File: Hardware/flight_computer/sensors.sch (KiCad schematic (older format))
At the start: 4 parts

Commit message: added parts for DAN <3
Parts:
- J?: symbol openDrone_parts:DF40C2.0-20DS-0.4V51 -> flight_computer-rescue:DF40C2.0-20DS-0.4V51-openDrone_parts
- U?: symbol openDrone_parts:LIS3MDLTR -> flight_computer-rescue:LIS3MDLTR-openDrone_parts
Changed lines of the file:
@@
 Connection ~ 7800 5000
 $Comp
-L openDrone_parts:DF40C2.0-20DS-0.4V51 J?
+L flight_computer-rescue:DF40C2.0-20DS-0.4V51-openDrone_parts J?
 U 1 1 5F6366CC
 P 2800 5150
@@
 	4500 6050 3500 6050
 $Comp
-L openDrone_parts:LIS3MDLTR U?
+L flight_computer-rescue:LIS3MDLTR-openDrone_parts U?
 U 1 1 5F647DF8
 P 7300 2500

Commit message: added more parts and datasheets
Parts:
- J?: symbol flight_computer-rescue:DF40C2.0-20DS-0.4V51-openDrone_parts -> flight_computer-rescue:DF40C2.0-20DS-0.4V51-openDrone_parts-flight_computer-rescue
- U?: symbol flight_computer-rescue:LIS3MDLTR-openDrone_parts -> flight_computer-rescue:LIS3MDLTR-openDrone_parts-flight_computer-rescue
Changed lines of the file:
@@
 Connection ~ 7800 5000
 $Comp
-L flight_computer-rescue:DF40C2.0-20DS-0.4V51-openDrone_parts J?
+L flight_computer-rescue:DF40C2.0-20DS-0.4V51-openDrone_parts-flight_computer-rescue J?
 U 1 1 5F6366CC
 P 2800 5150
@@
 	4500 6050 3500 6050
 $Comp
-L flight_computer-rescue:LIS3MDLTR-openDrone_parts U?
+L flight_computer-rescue:LIS3MDLTR-openDrone_parts-flight_computer-rescue U?
 U 1 1 5F647DF8
 P 7300 2500

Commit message: Adds sensors
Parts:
- removed J?: DF40C2.0-20DS-0.4V51, drone_footprints:DF40C2.0-20DS-0.4V51, symbol flight_computer-rescue:DF40C2.0-20DS-0.4V51-openDrone_parts-flight_computer-res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
- removed U?: MPU-6000, Sensor_Motion:InvenSense_QFN-24_4x4mm_P0.5mm, symbol Sensor_Motion:MPU-6000
- removed U?: MS5611-01BA, Package_LGA:LGA-8_3x5mm_P1.25mm, symbol Sensor_Pressure:MS5611-01BA
- removed U?: LIS3MDLTR, drone_footprints:LIS3MDLTR, symbol flight_computer-rescue:LIS3MDLTR-openDrone_parts-flight_computer-rescue
- added C? (x6): C_0u1, Capacitors_SMD:C_0805, symbol openDrone_parts:C_0u1
- added C?: C_1u, Capacitors_SMD:C_0805, symbol openDrone_parts:C_1u
- added C?: C_10u, Capacitors_SMD:C_0805, symbol openDrone_parts:C_10u
- added C?: C_2u2, Capacitors_SMD:C_0805, symbol openDrone_parts:C_2u2
- added R?: R_220, Resistors_SMD:R_0805, symbol openDrone_parts:R_220
- added U?: BMI088, drone_footprints:BMI088, symbol openDrone_parts:BMI088
- added U?: LIS3MDLTR, drone_footprints:LIS3MDLTR, symbol openDrone_parts:LIS3MDLTR
- added U?: Barometer, drone_footprints:MS561101BA03-50, symbol openDrone_parts:Barometer
- added U?: LP5907QMFX-3.3, TO_SOT_Packages_SMD:SOT-23-5, symbol openDrone_parts:LP5907QMFX-3.3
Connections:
- net labels added: BARO_MISO, BARO_MOSI, BARO_SCK, CSB_ACCEL, CSB_GYRO, IMU_INT1_ACCEL, IMU_INT2_ACCEL, IMU_MISO, IMU_MOSI, IMU_SCK, INT3_GYRO, INT4_GYRO, MAG_CS, MAG_DRDY, MAG_INT, MAG_SCL, MAG_SDA_SDI_SDO, MAG_SDO_SA1, VDDIO, VDD_3V3_SENSORS_EN, VDD_5V
- net labels removed: ACCEL_MAG_EXT_CS, BARO_EXT_CS, GYRO_EXT_CS, IMU_TEMPERATURE_CONTROL, MPU_CS, MPU_EXT_CS, SPI_EXT_MISO, SPI_EXT_MOSI, SPI_EXT_SCK, SPI_INT_MISO, SPI_INT_MOSI, SPI_INT_SCK
- wire segments 43 -> 53

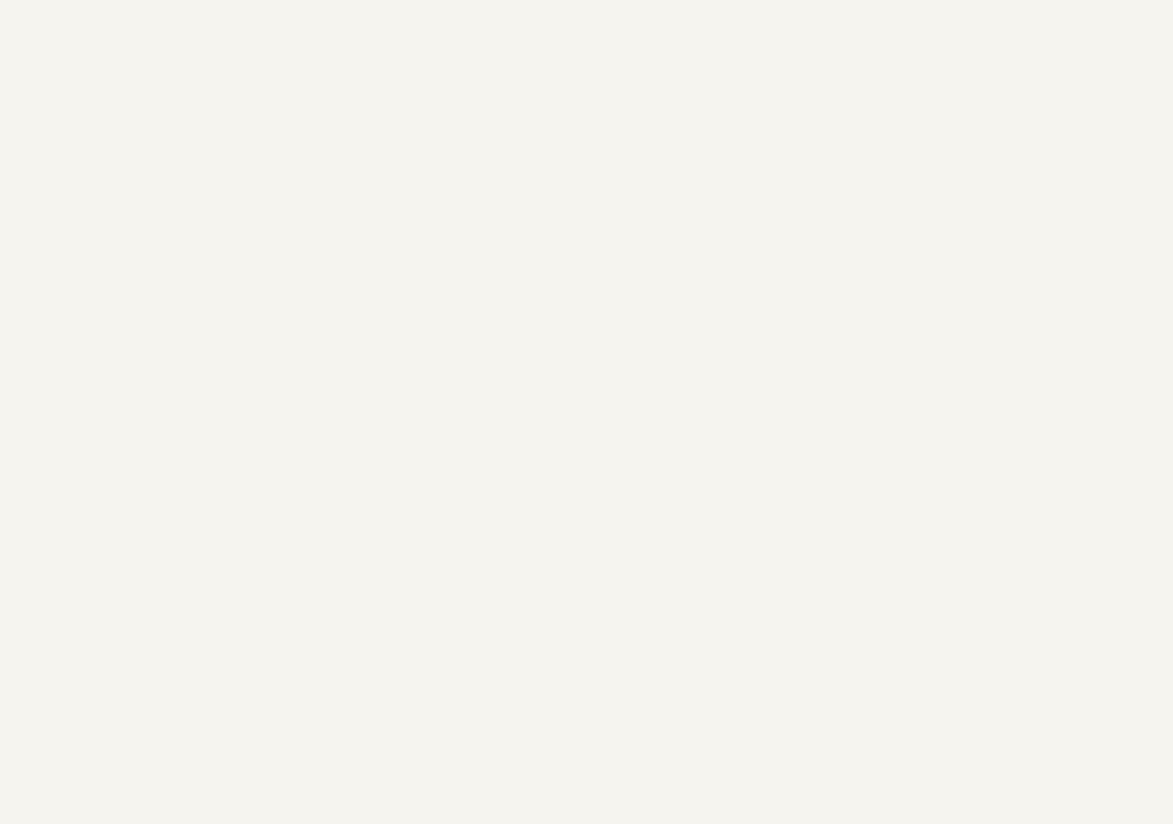
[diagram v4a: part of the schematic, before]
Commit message: Adds more sensor connections and communication with stm
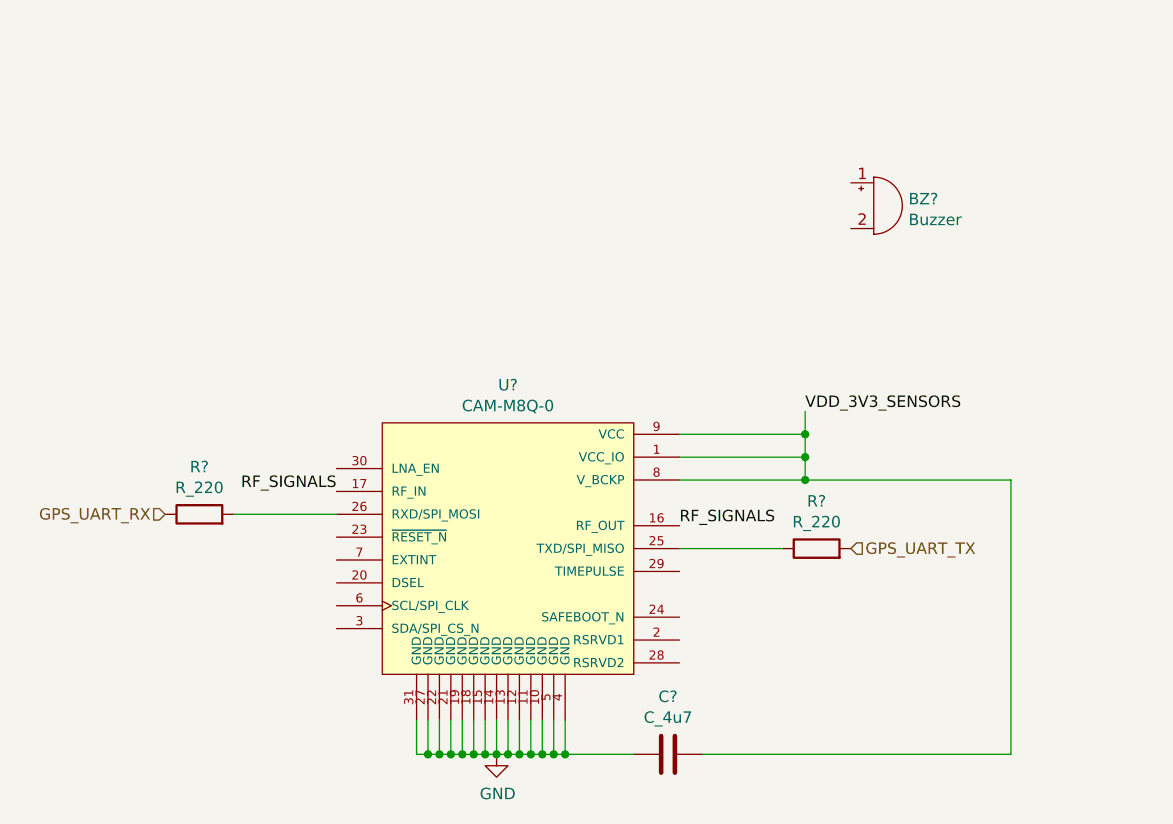
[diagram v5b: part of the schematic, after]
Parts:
- added BZ?: Buzzer, drone_footprints:PT-2040PQ, symbol openDrone_parts:Buzzer
- added C?: C_4u7, Capacitors_SMD:C_0805, symbol openDrone_parts:C_4u7
- added R? (x2): R_220, Resistors_SMD:R_0805, symbol openDrone_parts:R_220
- added U?: CAM-M8Q-0, drone_footprints:CAM_M8Q_0, symbol openDrone_parts:CAM-M8Q-0
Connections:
- net GND: now also C?.2, U?.10 (GND), U?.11 (GND), U?.12 (GND), U?.13 (GND), U?.14 (GND), U?.15 (GND), U?.18 (GND), U?.19 (GND), U?.21 (GND), U?.22 (GND), U?.27 (GND), U?.31 (GND), U?.4 (GND), U?.5 (GND)
- net VDD_3V3_SENSORS: now also C?.1, U?.1 (VCC_IO), U?.8 (V_BCKP), U?.9 (VCC)
- new net: R?.1, U?.25 (TXD/SPI_MISO)
- new net: R?.2, U?.26 (RXD/SPI_MOSI)
- new net GPS_UART_RX: R?.1
- new net GPS_UART_TX: R?.2
- new net RF_SIGNALS: U?.16 (RF_OUT), U?.17 (RF_IN)
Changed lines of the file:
@@
 $Descr A4 11693 8268
 encoding utf-8
-Sheet 2 5
+Sheet 2 4
 Title ""
 Date ""
@@
 Text Label 10400 4150 0    50   ~ 0
 VDD_3V3_SENSORS
+$Comp
+L openDrone_parts:Buzzer BZ?
+U 1 1 5F827564
+P 4700 3500
+F 0 "BZ?" H 4852 3529 50  0000 L CNN
+F 1 "Buzzer" H 4852 3438 50  0000 L CNN
+F 2 "drone_footprints:PT-2040PQ" H 5050 3950 50  0001 C CNN
+F 3 "~" V 4675 3600 50  0001 C CNN
+F 4 "458-1078-ND" H 5000 3750 50  0001 C CNN "DPN"
+F 5 "PT-2040PQ" H 4950 3850 50  0001 C CNN "MPN"
+	1    4700 3500
+	1    0    0    -1
+$EndComp
+$Comp
+L openDrone_parts:CAM-M8Q-0 U?
+U 1 1 5F827FBC
+P 3100 4600
+F 0 "U?" H 3100 4915 50  0000 C CNN
+F 1 "CAM-M8Q-0" H 3100 4824 50  0000 C CNN
+F 2 "drone_footprints:CAM_M8Q_0" H 2650 4950 50  0001 L BNN
+F 3 "UBlox" H 3000 4850 50  0001 L BNN
+F 4 "672-CAM-M8Q-0CT-ND" H 3150 4850 50  0001 C CNN "DPN"
+	1    3100 4600
+	1    0    0    -1
+$EndComp
+$Comp
+L openDrone_parts:R_220 R?
+U 1 1 5F82A212
+P 4450 5000
+F 0 "R?" H 4450 5207 50  0000 C CNN
+F 1 "R_220" H 4450 5116 50  0000 C CNN
+F 2 "Resistors_SMD:R_0805" H 3650 5150 50  0001 C CNN
+F 3 "" H 4150 5500 50  0001 C CNN
+F 4 "311-220CRCT-ND" H 3800 5250 60  0001 C CNN "DPN"
+	1    4450 5000
+	1    0    0    -1
+$EndComp
+$Comp
+L openDrone_parts:R_220 R?
+U 1 1 5F82B7EB
+P 1750 4850
+F 0 "R?" H 1750 5057 50  0000 C CNN
+F 1 "R_220" H 1750 4966 50  0000 C CNN
+F 2 "Resistors_SMD:R_0805" H 950 5000 50  0001 C CNN
+F 3 "" H 1450 5350 50  0001 C CNN
+F 4 "311-220CRCT-ND" H 1100 5100 60  0001 C CNN "DPN"
+	1    1750 4850
+	1    0    0    -1
+$EndComp
+Text HLabel 4600 5000 2    50   Input ~ 0
+GPS_UART_TX
+Text HLabel 1600 4850 0    50   Input ~ 0
+GPS_UART_RX
+$Comp
+L power:GND #PWR?
+U 1 1 5F857A76
+P 3050 5900
+F 0 "#PWR?" H 3050 5650 50  0001 C CNN
+F 1 "GND" H 3055 5727 50  0000 C CNN
+F 2 "" H 3050 5900 50  0001 C CNN
+F 3 "" H 3050 5900 50  0001 C CNN
+	1    3050 5900
+	1    0    0    -1
+$EndComp
+Wire Wire Line
+	2700 5750 2700 5900
+Wire Wire Line
+	2700 5900 2750 5900
+Wire Wire Line
+	3350 5750 3350 5900
+Wire Wire Line
+	3350 5900 3300 5900
+Connection ~ 3050 5900
+Wire Wire Line
+	3300 5750 3300 5900
+Connection ~ 3300 5900
+Wire Wire Line
+	3300 5900 3250 5900
+Wire Wire Line
+	3250 5750 3250 5900
+Connection ~ 3250 5900
+Wire Wire Line
+	3250 5900 3200 5900
+Wire Wire Line
+	3200 5750 3200 5900
+Connection ~ 3200 5900
+Wire Wire Line
+	3200 5900 3150 5900
+Wire Wire Line
+	3150 5750 3150 5900
+Connection ~ 3150 5900
+Wire Wire Line
+	3150 5900 3100 5900
+Wire Wire Line
+	3100 5750 3100 5900
+Connection ~ 3100 5900
+Wire Wire Line
+	3100 5900 3050 5900
+Wire Wire Line
+	3050 5750 3050 5900
+Wire Wire Line
+	3000 5750 3000 5900
+Connection ~ 3000 5900
+Wire Wire Line
+	3000 5900 3050 5900
+Wire Wire Line
+	2950 5750 2950 5900
+Connection ~ 2950 5900
+Wire Wire Line
+	2950 5900 3000 5900
+Wire Wire Line
+	2900 5750 2900 5900
+Connection ~ 2900 5900
+Wire Wire Line
+	2900 5900 2950 5900
+Wire Wire Line
+	2850 5750 2850 5900
+Connection ~ 2850 5900
+Wire Wire Line
+	2850 5900 2900 5900
+Wire Wire Line
+	2800 5750 2800 5900
+Connection ~ 2800 5900
+Wire Wire Line
+	2800 5900 2850 5900
+Wire Wire Line
+	2750 5750 2750 5900
+Connection ~ 2750 5900
+Wire Wire Line
+	2750 5900 2800 5900
+Text Label 2350 4750 2    50   ~ 0
+RF_SIGNALS
+Wire Wire Line
+	1900 4850 2350 4850
+Text Label 3850 4900 0    50   ~ 0
+RF_SIGNALS
+Wire Wire Line
+	3850 5000 4300 5000
+Text Label 4400 4400 0    50   ~ 0
+VDD_3V3_SENSORS
+Wire Wire Line
+	3850 4500 4400 4500
+Wire Wire Line
+	4400 4500 4400 4400
+Wire Wire Line
+	3850 4600 4400 4600
+Wire Wire Line
+	4400 4600 4400 4500
+Connection ~ 4400 4500
+Wire Wire Line
+	3850 4700 4400 4700
+Wire Wire Line
+	4400 4700 4400 4600
+Connection ~ 4400 4600
+$Comp
+L openDrone_parts:C_4u7 C?
+U 1 1 5F87B412
+P 3800 5900
+F 0 "C?" V 3548 5900 50  0000 C CNN
+F 1 "C_4u7" V 3639 5900 50  0000 C CNN
+F 2 "Capacitors_SMD:C_0805" H 3838 5750 50  0001 C CNN
+F 3 "" H 3825 6000 50  0001 C CNN
+F 4 "490-14466-1-ND" H 3800 5900 60  0001 C CNN "DPN"
+	1    3800 5900
+	0    1    1    0
+$EndComp
+Wire Wire Line
+	3350 5900 3650 5900
+Connection ~ 3350 5900
+Wire Wire Line
+	3950 5900 5300 5900
+Wire Wire Line
+	5300 5900 5300 4700
+Wire Wire Line
+	5300 4700 4400 4700
+Connection ~ 4400 4700
 $EndSCHEMATC

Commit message: Updates drdy pins and rc connections
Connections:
- net IMU_INT2_ACCEL: no longer names the net of U?.1 (INT2)
- net INT4_GYRO: no longer names the net of U?.13 (INT4)
- net MAG_INT: no longer names the net of U?.7 (INT)
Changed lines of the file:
@@
 Text HLabel 3850 1000 2    50   Input ~ 0
 IMU_INT1_ACCEL
-Text HLabel 3850 1100 2    50   Input ~ 0
-IMU_INT2_ACCEL
 Text HLabel 3850 1200 2    50   Input ~ 0
 INT3_GYRO
-Text HLabel 3850 1300 2    50   Input ~ 0
-INT4_GYRO
 Wire Wire Line
 	3850 1500 3950 1500
@@
 	2700 2450 2900 2450
 Connection ~ 2900 2450
-$Comp
-L openDrone_parts:LIS3MDLTR U?
-U 1 1 5F9477A8
-P 6450 1150
-F 0 "U?" H 7400 1437 60  0000 C CNN
-F 1 "LIS3MDLTR" H 7400 1331 60  0000 C CNN
-F 2 "drone_footprints:LIS3MDLTR" H 7650 1390 60  0001 C CNN
-F 3 "https://www.st.com/content/ccc/resource/technical/document/datasheet/54/2a/85/76/e3/97/42/18/DM00075867.pdf/files/DM00075867.pdf/jcr:content/translations/en.DM00075867.pdf" H 6450 1150 60  0001 C CNN
-F 4 "497-13892-1-ND" H 8400 1500 50  0001 C CNN "DPN"
-	1    6450 1150
-	1    0    0    -1
-$EndComp
 Text HLabel 6450 1650 0    50   Input ~ 0
 VDDIO
@@
 Text HLabel 8350 1550 2    50   Input ~ 0
 MAG_DRDY
-Text HLabel 8350 1650 2    50   Input ~ 0
-MAG_INT
 Text HLabel 8350 1350 2    50   Input ~ 0
 MAG_CS
@@
 	5300 4700 4400 4700
 Connection ~ 4400 4700
+$Comp
+L openDrone_parts:LIS3MDLTR U?
+U 1 1 5F9477A8
+P 6450 1150
+F 0 "U?" H 7400 1437 60  0000 C CNN
+F 1 "LIS3MDLTR" H 7400 1331 60  0000 C CNN
+F 2 "drone_footprints:LIS3MDLTR" H 7650 1390 60  0001 C CNN
+F 3 "https://www.st.com/content/ccc/resource/technical/document/datasheet/54/2a/85/76/e3/97/42/18/DM00075867.pdf/files/DM00075867.pdf/jcr:content/translations/en.DM00075867.pdf" H 6450 1150 60  0001 C CNN
+F 4 "497-13892-1-ND" H 8400 1500 50  0001 C CNN "DPN"
+	1    6450 1150
+	1    0    0    -1
+$EndComp
 $EndSCHEMATC

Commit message: Adds buck converters
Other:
- note added: "GPS\n<71mA, avg <26mA"
- note added: "IMU\n150uA"
- note added: "Magnetometer\n40-270uA"
- note added: "barometer\n<1.4mA"
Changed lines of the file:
@@
 	1    0    0    -1
 $EndComp
+Text Notes 7100 2000 0    50   ~ 0
+Magnetometer\n40-270uA
+Text Notes 3900 1800 0    50   ~ 0
+IMU\n150uA
+Text Notes 1750 5750 0    50   ~ 0
+GPS\n<71mA, avg <26mA
+Text Notes 9150 3500 0    50   ~ 0
+barometer\n<1.4mA
 $EndSCHEMATC

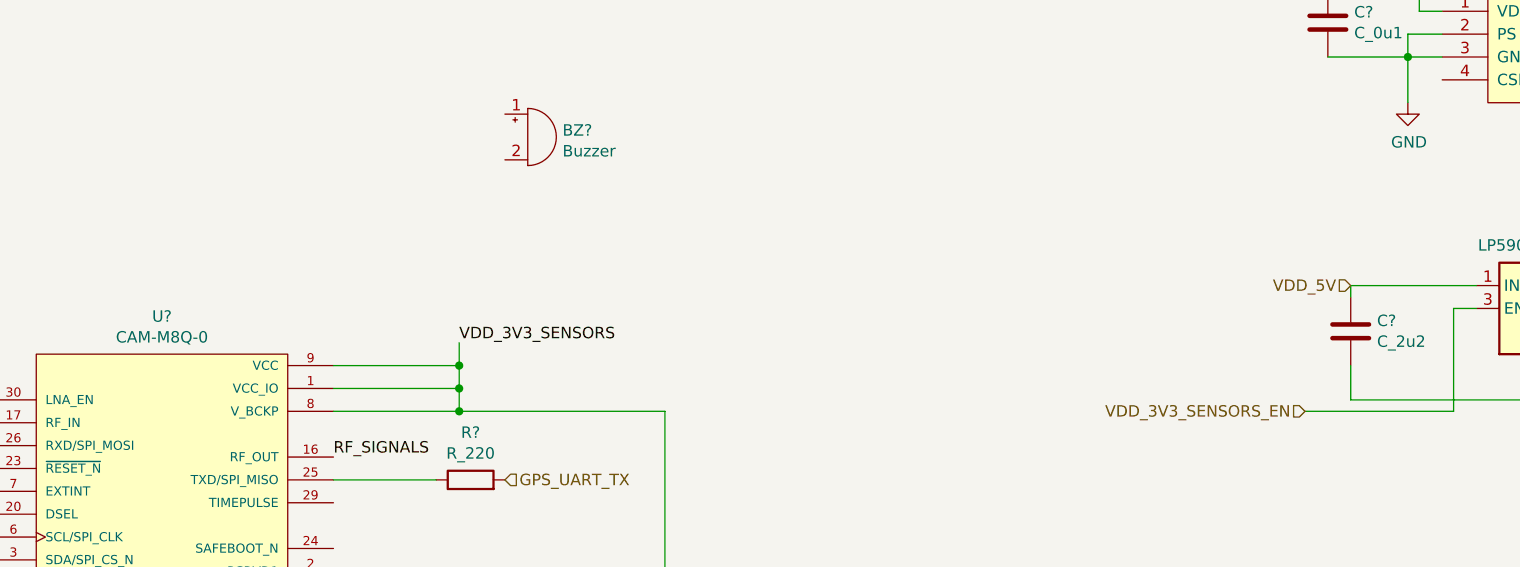
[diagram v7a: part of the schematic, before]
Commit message: Adds in regulators and filters
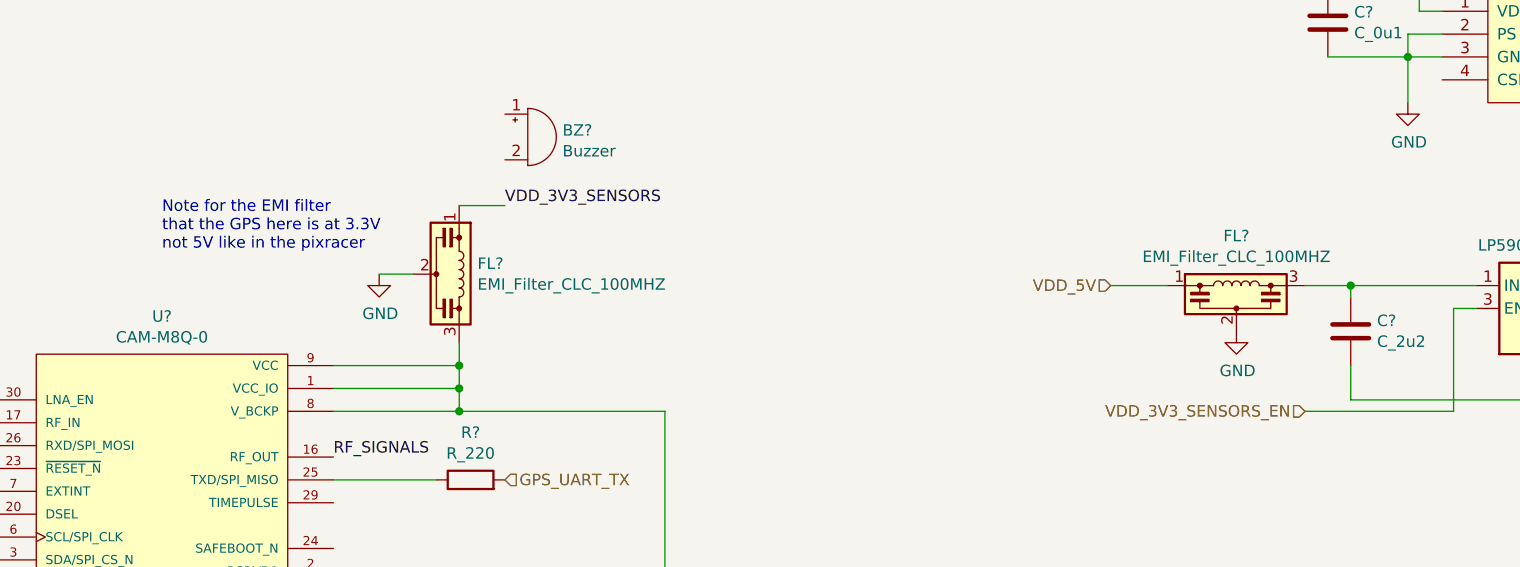
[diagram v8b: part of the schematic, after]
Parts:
- added FL? (x2): EMI_Filter_CLC_100MHZ, drone_footprints:NFL21SP107X1C3D, symbol openDrone_parts:EMI_Filter_CLC_100MHZ
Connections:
- net GND: now also FL?.2, FL?.2
- net VDD_3V3_SENSORS: now also FL?.1; no longer C?.1, U?.1 (VCC_IO), U?.8 (V_BCKP), U?.9 (VCC)
- net VDD_5V: now also FL?.1; no longer C?.1, U?.1 (IN)
- new net: C?.1, FL?.3, U?.1 (VCC_IO), U?.8 (V_BCKP), U?.9 (VCC)
- new net: C?.1, FL?.3, U?.1 (IN)
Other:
- note added: "Note for the EMI filter \nthat the GPS here is at 3.3V \nnot 5V like in the pixracer"
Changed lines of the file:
@@
 Wire Wire Line
 	9150 4650 9150 4750
-Text HLabel 8300 4150 0    50   Input ~ 0
+Text HLabel 7250 4150 0    50   Input ~ 0
 VDD_5V
 Text Label 2700 2450 2    50   ~ 0
@@
 F 1 "CAM-M8Q-0" H 3100 4824 50  0000 C CNN
 F 2 "drone_footprints:CAM_M8Q_0" H 2650 4950 50  0001 L BNN
-F 3 "UBlox" H 3000 4850 50  0001 L BNN
+F 3 "https://www.u-blox.com/sites/default/files/CAM-M8-FW3_DataSheet_%28UBX-15031574%29.pdf" H 3000 4850 50  0001 L BNN
 F 4 "672-CAM-M8Q-0CT-ND" H 3150 4850 50  0001 C CNN "DPN"
 	1    3100 4600
@@
 Wire Wire Line
 	3850 5000 4300 5000
-Text Label 4400 4400 0    50   ~ 0
+Text Label 4600 3800 0    50   ~ 0
 VDD_3V3_SENSORS
 Wire Wire Line
@@
 Text Notes 9150 3500 0    50   ~ 0
 barometer\n<1.4mA
+$Comp
+L openDrone_parts:EMI_Filter_CLC_100MHZ FL?
+U 1 1 5F9362EA
+P 4300 4100
+F 0 "FL?" V 4254 4280 50  0000 L CNN
+F 1 "EMI_Filter_CLC_100MHZ" V 4345 4280 50  0000 L CNN
+F 2 "drone_footprints:NFL21SP107X1C3D" H 4950 4600 50  0001 C CNN
+F 3 "" V 4300 4100 50  0001 C CNN
+F 4 "490-2540-1-ND" H 5200 4350 50  0001 C CNN "DPN"
+F 5 "NFL21SP107X1C3D" H 4950 4450 50  0001 C CNN "MPN"
+	1    4300 4100
+	0    1    1    0
+$EndComp
+Wire Wire Line
+	4600 3800 4400 3800
+$Comp
+L power:GND #PWR?
+U 1 1 5F93AFA7
+P 4050 4100
+F 0 "#PWR?" H 4050 3850 50  0001 C CNN
+F 1 "GND" H 4055 3927 50  0000 C CNN
+F 2 "" H 4050 4100 50  0001 C CNN
+F 3 "" H 4050 4100 50  0001 C CNN
+	1    4050 4100
+	1    0    0    -1
+$EndComp
+Wire Wire Line
+	4200 4100 4050 4100
+Text Notes 3100 4000 0    50   ~ 0
+Note for the EMI filter \nthat the GPS here is at 3.3V \nnot 5V like in the pixracer
+$Comp
+L openDrone_parts:EMI_Filter_CLC_100MHZ FL?
+U 1 1 5FA22B48
+P 7800 4250
+F 0 "FL?" H 7800 4567 50  0000 C CNN
+F 1 "EMI_Filter_CLC_100MHZ" H 7800 4476 50  0000 C CNN
+F 2 "drone_footprints:NFL21SP107X1C3D" H 8450 4750 50  0001 C CNN
+F 3 "" V 7800 4250 50  0001 C CNN
+F 4 "490-2540-1-ND" H 8700 4500 50  0001 C CNN "DPN"
+F 5 "NFL21SP107X1C3D" H 8450 4600 50  0001 C CNN "MPN"
+	1    7800 4250
+	1    0    0    -1
+$EndComp
+Wire Wire Line
+	8300 4150 8100 4150
+Connection ~ 8300 4150
+$Comp
+L power:GND #PWR?
+U 1 1 5FA26F34
+P 7800 4350
+F 0 "#PWR?" H 7800 4100 50  0001 C CNN
+F 1 "GND" H 7805 4177 50  0000 C CNN
+F 2 "" H 7800 4350 50  0001 C CNN
+F 3 "" H 7800 4350 50  0001 C CNN
+	1    7800 4350
+	1    0    0    -1
+$EndComp
+Wire Wire Line
+	7250 4150 7500 4150
 $EndSCHEMATC
